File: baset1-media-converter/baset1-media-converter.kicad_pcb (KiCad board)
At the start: 4 copper layers, 181 parts, among them J1 CONN_01X05, J2 UX60SX-MB-5ST, J3 0826-1G1T-23-F, J4 CONN_01X02, M1 LOGO, M2 LOGO, M3 LOGO, Q1 SSM6N58NU, U1 STM32F031-QFN28, U10 NCP45521-H, U2 FT234XD, U3 LTC3374-QFN, U4 KSZ9031RN, U5 ECS-1612MV-250-CN, U6 RCLAMP0514M, U7 RCLAMP0514M, U8 DP83TG720S-Q1, U9 ECS-1612MV-250-CN

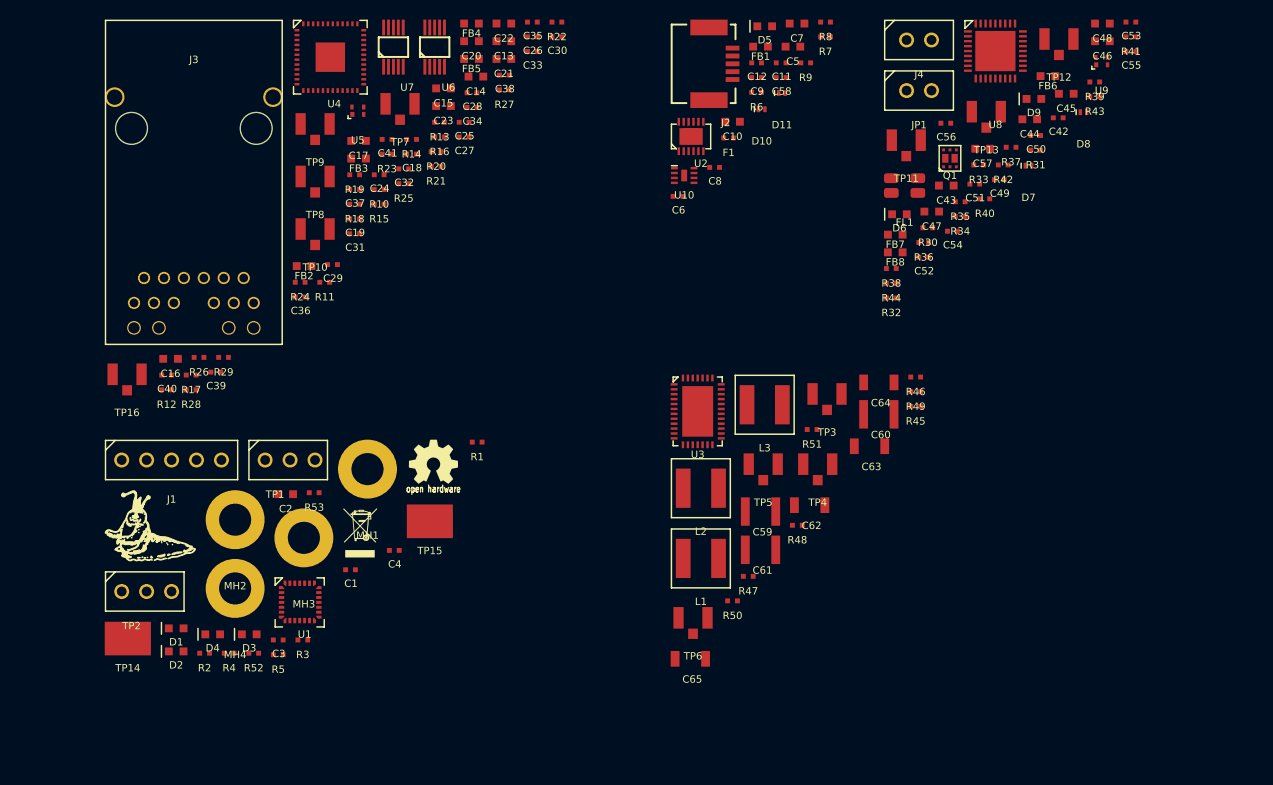
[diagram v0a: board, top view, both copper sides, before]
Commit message: Continued layout on media converter
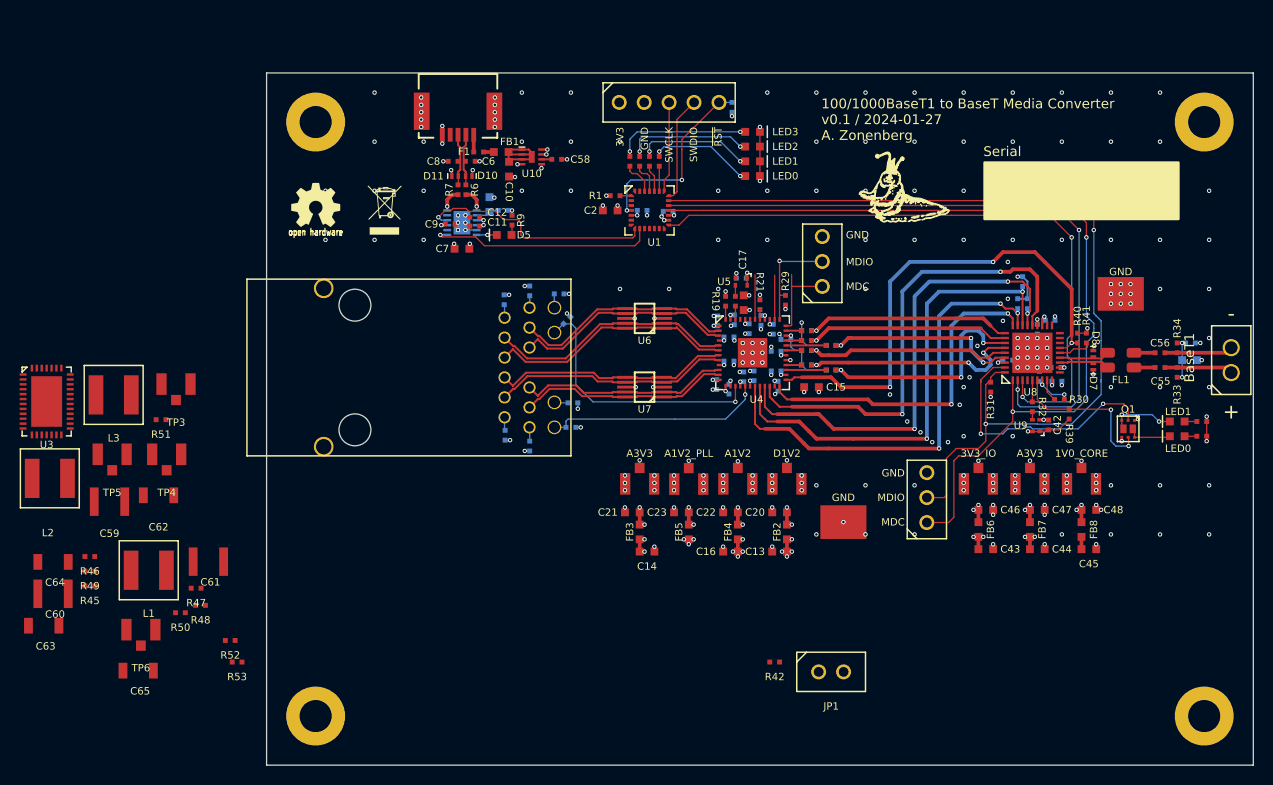
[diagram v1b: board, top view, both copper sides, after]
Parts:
- removed TP16: U.FL, azonenberg_pcb:CONN_U.FL_TE_1909763-1
- C1, C18, C19, C24, C25, C26, C27, C28, C29, C3, C30, C31, C32, C33, C34, C35, C36, C37, C38, C39, C4, C40, C41, C49, C5, C50, C51, C52, C53, C54, C57, R10, R11, R12, R20, R23, R24, R25, R26, R27, R28, R35, R36, R37, R38, R8, U2: moved to B.Cu
- moved TP14 107.0 mm to (156.0, 60.5)
- moved MH2 106.7 mm to (164.5, 43.0)
- moved MH4 99.6 mm to (164.5, 103.5)
- moved C60 86.1 mm to (47.2, 91.0)
- moved C64 86.1 mm to (47.2, 87.8)
- moved R45 86.1 mm to (51.0, 90.2)
- moved R46 86.1 mm to (51.0, 87.2)
- moved R49 86.1 mm to (51.0, 88.8)
- moved C63 86.1 mm to (46.3, 94.3)
- moved M1 84.2 mm to (134.5, 50.0)
- moved TP2 80.0 mm to (136.2, 81.2), turned to 90 degrees
- moved D2 77.1 mm to (118.5, 47.0), turned to 180 degrees
- moved D4 75.1 mm to (118.5, 44.0), turned to 180 degrees
- moved D1 74.6 mm to (118.5, 48.5), turned to 180 degrees
- moved D3 71.4 mm to (118.5, 45.5), turned to 180 degrees
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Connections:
- FL1 pad 1: /BaseT1 PHY/SPE_1_P -> /BaseT1 PHY/SPE_1_N
- FL1 pad 2: /BaseT1 PHY/SPE_2_P -> /BaseT1 PHY/SPE_2_N
- FL1 pad 3: /BaseT1 PHY/SPE_1_N -> /BaseT1 PHY/SPE_1_P
- FL1 pad 4: /BaseT1 PHY/SPE_2_N -> /BaseT1 PHY/SPE_2_P
- U1 pad 14: /LED0 -> /1V2_EN
- U1 pad 15: /LED1 -> /SPE_RST_N
- U1 pad 18: /1V2_EN -> /SPE_INT_N
- U1 pad 19: /BASET_INT_N -> /SPE_MDC
- U1 pad 20: /SPE_INT_N -> /SPE_MDIO
- U1 pad 23: unconnected-(U1-Pad23) -> /LED0
- U1 pad 24: /LED2 -> /LED1
- U1 pad 25: /LED3 -> /LED2
- U1 pad 26: /SPE_MDIO -> /LED3
- U1 pad 27: /SPE_MDC -> unconnected-(U1-Pad27)
- U1 pad 28: /SPE_RST_N -> /BASET_INT_N
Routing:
- net /GND: track 0.00 -> 540.8 mm, vias 0 -> 257
- net /3V3: track 0.00 -> 275.6 mm, vias 0 -> 29
- net /SPE_MDIO: track 0.00 -> 94.7 mm, vias 0 -> 2
- net /SPE_MDC: track 0.00 -> 90.5 mm, vias 0 -> 2
- net /5V0: track 0.00 -> 77.0 mm, vias 0 -> 3
- net /SPE_INT_N: track 0.00 -> 69.0 mm, vias 0 -> 2
- net /SPE_RST_N: track 0.00 -> 66.3 mm, vias 0 -> 2
- net /BaseT1 PHY/SPE_RX_DV: track 0.00 -> 50.6 mm, vias 0 -> 3
- net /BaseT1 PHY/SPE_RXD1: track 0.00 -> 48.8 mm, vias 0 -> 2
- net /BaseT1 PHY/SPE_RXD2: track 0.00 -> 48.8 mm, vias 0 -> 3
- net /BaseT PHY/BASET_TXD3: track 0.00 -> 48.0 mm, vias 0 -> 2
- net /BaseT1 PHY/SPE_RXD0: track 0.00 -> 47.8 mm, vias 0 -> 3
- net /BaseT PHY/A3V3: track 0.00 -> 42.8 mm, vias 0 -> 8
- net /BaseT PHY/D1V2: track 0.00 -> 39.1 mm, vias 0 -> 10
- net /BaseT PHY/BASET_TX_CLK: track 0.00 -> 34.3 mm, vias 0 -> 2
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- added copper zone on In1.Cu, net /GND
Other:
- board outline added: 100.5 x 70.5 mm
- board text added: "+"
- board text added: "-"
- board text added: "100/1000BaseT1 to BaseT Media Converter v0.1 / 2024-01-27 A. Zonenberg"
- board text added: "1V0_CORE"
- board text added: "3V3"
- board text added: "3V3_IO"
- board text added: "A1V2"
- board text added: "A1V2_PLL"
- board text added: "A3V3"
- board text added: "BaseT1"
- board text added: "D1V2"
- board text added: "GND"
- board text added: "LED0"
- board text added: "LED1"
- board text added: "LED2"
- board text added: "LED3"
- board text added: "MDC"
- board text added: "MDIO"
- board text added: "SWCLK"
- board text added: "SWDIO"
- board text added: "Serial"
- board text added: "~{RST}"

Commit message: Updating file: baset1-media-converter.kicad_pcb with current fully routed design
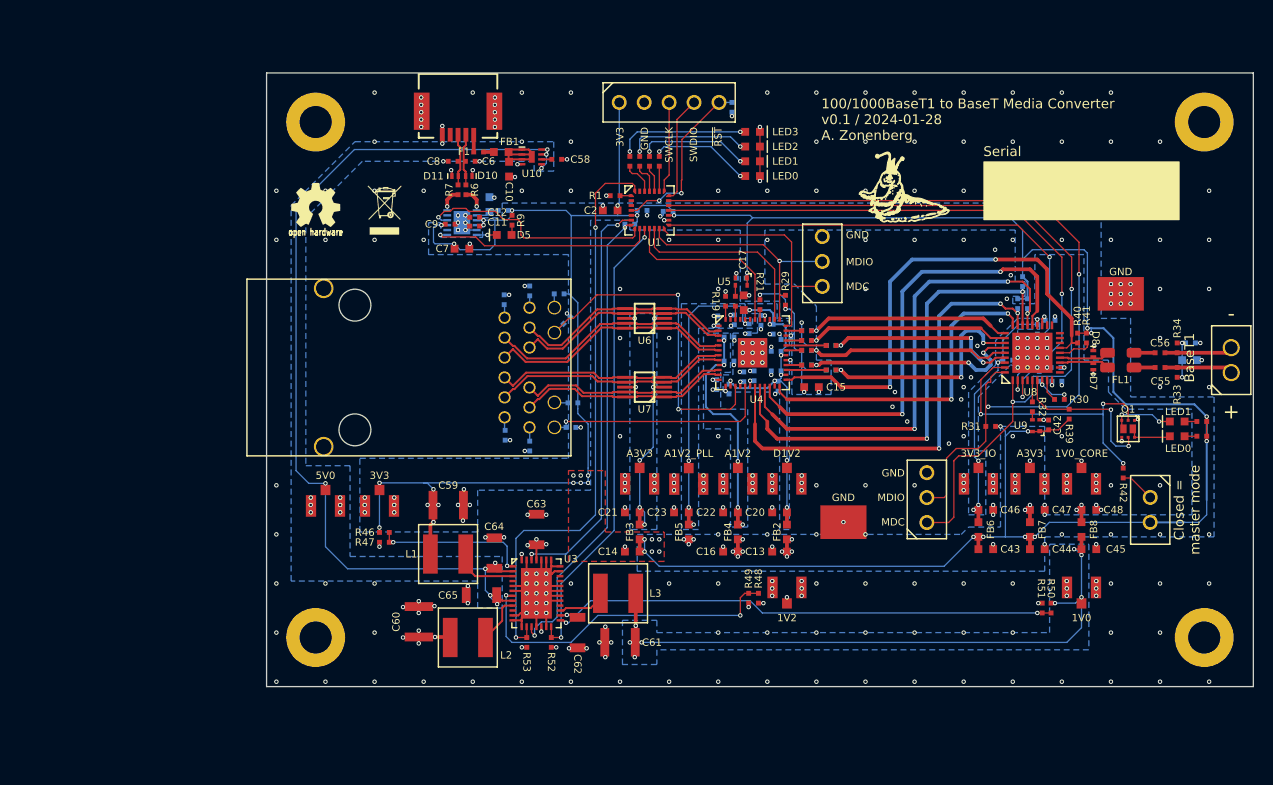
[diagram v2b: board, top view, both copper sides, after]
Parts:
- R45: moved to B.Cu
- moved TP6 95.9 mm to (152.0, 90.5)
- moved R51 91.8 mm to (148.0, 92.5), turned to -90 degrees
- moved R50 88.7 mm to (148.9, 92.5), turned to -90 degrees
- moved TP5 70.0 mm to (122.0, 90.5)
- moved R49 67.2 mm to (118.1, 91.5), turned to 90 degrees
- moved R45 66.2 mm to (106.0, 53.4)
- moved R48 56.8 mm to (119.1, 91.5), turned to 90 degrees
- moved L3 55.2 mm to (104.8, 91.0), turned to 180 degrees
- moved U3 53.6 mm to (96.5, 91.0)
- moved C63 51.1 mm to (96.5, 84.5), turned to 90 degrees
- moved L2 45.6 mm to (89.5, 95.5)
- moved C64 44.9 mm to (92.2, 86.9), turned to 90 degrees
- moved C62 44.9 mm to (100.7, 95.0), turned to -90 degrees
- moved C61 42.7 mm to (105.0, 96.0), turned to 180 degrees
- moved R42 40.4 mm to (156.2, 78.7), turned to -90 degrees
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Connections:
- C62 pad 2: Net-(C62-Pad2) -> /GND
- C63 pad 2: Net-(C62-Pad2) -> /GND
- C64 pad 2: Net-(C62-Pad2) -> /GND
- C65 pad 2: Net-(C62-Pad2) -> /GND
- U1 pad 10: /BASET_MDIO -> /1V0_EN
- U1 pad 12: /BASET_MDC -> /BASET_INT_N
- U1 pad 13: /1V0_EN -> /BASET_MDIO
- U1 pad 14: /1V2_EN -> /BASET_MDC
- U1 pad 15: /SPE_RST_N -> /SPE_INT_N
- U1 pad 18: /SPE_INT_N -> /SPE_RST_N
- U1 pad 28: /BASET_INT_N -> /1V2_EN
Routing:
- net /GND: track 540.8 -> 695.9 mm, vias 257 -> 373
- net /1V0: track 1.25 -> 72.4 mm, vias 0 -> 8
- net /3V3: track 275.6 -> 342.4 mm, vias 29 -> 43
- net /1V2_EN: track 0.00 -> 59.2 mm, vias 0 -> 2
- net /1V2: track 24.8 -> 81.4 mm, vias 11 -> 17
- net /Power supply/1V0_FB: track 0.00 -> 51.6 mm, vias 0 -> 2
- net /PGOOD: track 0.00 -> 47.8 mm, vias 0 -> 2
- net /1V0_EN: track 0.00 -> 47.3 mm, vias 0 -> 2
- net /5V0: track 77.0 -> 121.5 mm, vias 3 -> 14
- net /VTEMP: track 0.00 -> 42.0 mm, vias 0 -> 2
- net /Power supply/1V2_FB: track 0.00 -> 34.0 mm, vias 0 -> 2
- net /BASET_MDC: track 8.93 -> 25.7 mm
- net /Power supply/3V3_FB: track 0.00 -> 15.8 mm, vias 0 -> 2
- net /BASET_INT_N: track 4.50 -> 20.2 mm
- net /BASET_RST_N: track 4.55 -> 18.7 mm
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- added copper zone on B.Cu, net /1V0
- added copper zone on In2.Cu, net /1V2
- added copper zone on B.Cu, net /3V3
- added copper zone on F.Cu, net /3V3
- added copper zone on In2.Cu, net /3V3
- added copper zone on B.Cu, net /5V0
- added copper zone on In2.Cu, net /5V0
- added copper zone on B.Cu, net /BaseT PHY/A1V2
- added copper zone on B.Cu, net /BaseT PHY/A1V2_PLL
- added copper zone on B.Cu, net /BaseT PHY/A3V3
- added copper zone on In2.Cu, net /BaseT PHY/A3V3
- added copper zone on B.Cu, net /BaseT PHY/D1V2
- added copper zone on In2.Cu, net /BaseT1 PHY/1V0_CORE
- added copper zone on B.Cu, net /BaseT1 PHY/3V3_IO
- added copper zone on In2.Cu, net /BaseT1 PHY/A3V3
- added copper zone on In2.Cu, net /GND
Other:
- board size 100.5 x 70.5 mm -> 100.5 x 62.5 mm
- board text added: "100/1000BaseT1 to BaseT Media Converter v0.1 / 2024-01-28 A. Zonenberg"
- board text added: "1V0"
- board text added: "1V2"
- board text added: "5V0"
- board text added: "Closed = master mode"
- board text removed: "100/1000BaseT1 to BaseT Media Converter v0.1 / 2024-01-27 A. Zonenberg"

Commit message: Final v0.1 media converter design after layout review
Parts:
- moved R22 0.15 mm to (116.6, 61.2)
- moved R40 0.10 mm to (151.7, 65.0)
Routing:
- net /SPE_INT_N: track 56.8 -> 58.7 mm
- net /3V3: track 342.4 -> 344.0 mm
- net /BaseT1 PHY/1V0_CORE: track 29.1 -> 29.9 mm
- net /BaseT1 PHY/3V3_IO: track 28.0 -> 28.7 mm
- net /PGOOD: track 47.8 -> 47.1 mm
- net /SPE_RST_N: track 60.5 -> 61.1 mm
- net /GND: vias 373 -> 382
- added copper zone on B.Cu, net /GND
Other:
- board text added: "TX/RX"
